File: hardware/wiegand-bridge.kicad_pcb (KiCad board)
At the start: 4 copper layers, 90 x 95 mm, 195 parts, among them J1 USB-C, J10 READER D0 D1, J11 READER LED BEEP, J12 GND IN3, J13 IN4 GND, J14 DC IN, J15 RELAY NC NO, J16 RELAY COM, J17 W5500, J18 QWIIC, J19 EXPANSION, J2 6-36V IN, J20 RS485 A B, J21 RS485 12V GND, J3 READER PWR, J4 LiFePO4 + NTC, J5 OLED SOCKET, J6 TFT/EPD, J8 TAMPER EXT, J9 IN1 IN2, K1 SRD-05VDC-SL-C, Q1 2N7002, Q10 2N7002, Q11 AO3401A, Q12 AO3400A, Q2 2N7002, Q4 2N7002, Q5 AO3401A, Q6 FS8205A, Q7 2N7002, Q8 2N7002, Q9 2N7002, SW1 BOOT, SW2 RESET, SW3 TAMPER, U1 ESP32-S3-WROOM-1-N8R2, U10 LMV321, U2 LMR16020, U3 TPS63001, U4 SN74LVC2G17, U5 CN3058E, U6 MT3608, U7 DW01A, U8 TCA9535, U9 SP3485

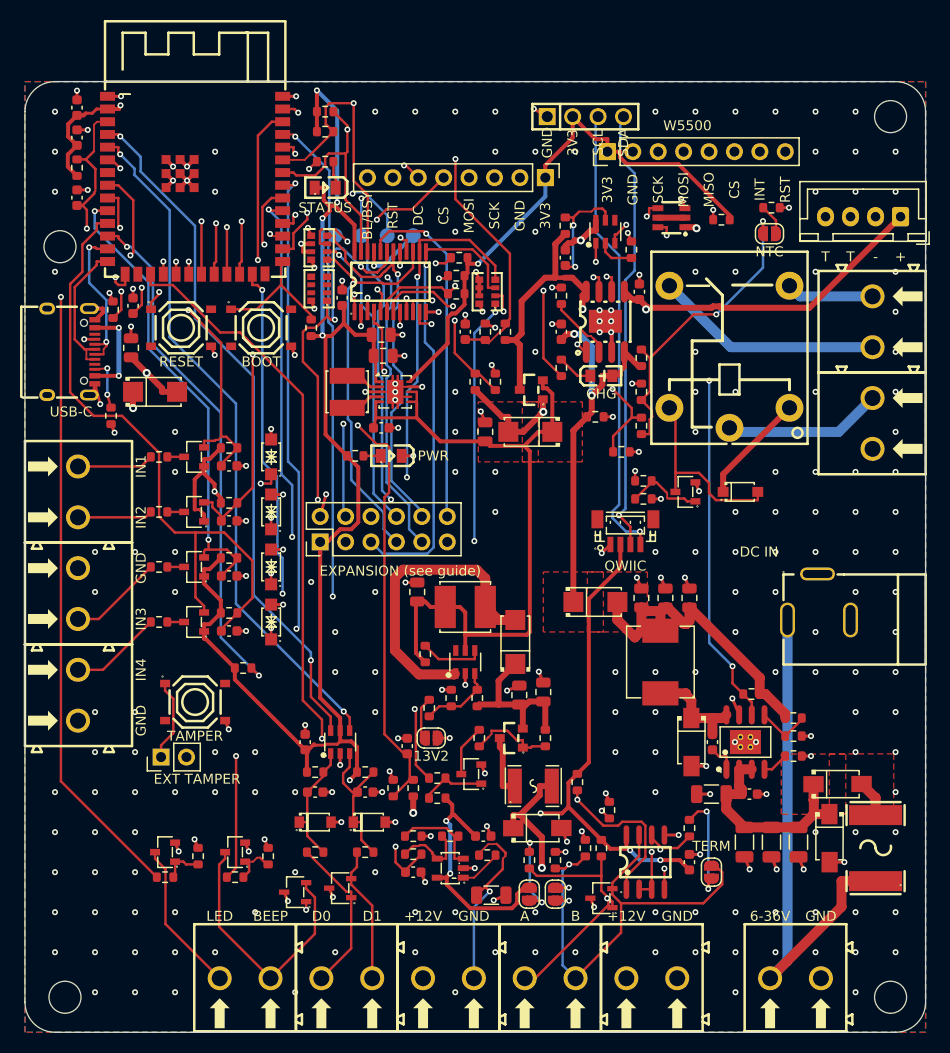
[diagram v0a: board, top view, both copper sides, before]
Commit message: Revision 11: red/green status pair and silkscreen legibility (routed and checked, not yet ordered)
Rev 10 is built and tested and stays available as tag rev-10b.
- D8 becomes red FAULT (IO21, ESPHome's status LED); new D23 green OK on IO47 via R81, lit while
  Home Assistant is connected. DISP_RST moves from IO47 to expander P06 (shared with J19 pin 3).
- Every silkscreen label held clear of pads, outlines, fitted parts and other text; audit.py --silk
  checks it (rev 10 had 41 problems in 70 labels). stitch.py keeps vias out of through-hole pads.
- Fab outputs and renders regenerated; the schematic PDF title now says revision 11.
- Firmware drives the OK LED (harmless on rev 10, where IO47 reaches only the unfitted J6).
- docs/design.md and README describe the changes.
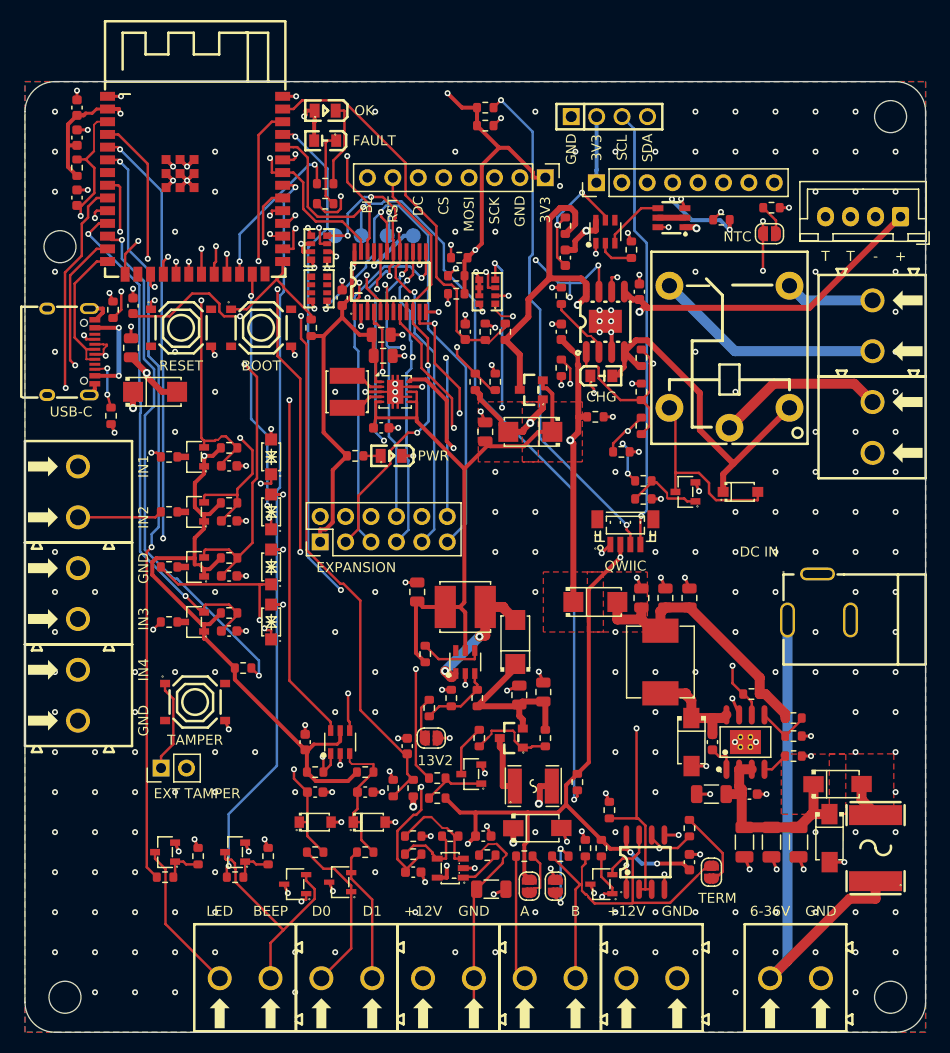
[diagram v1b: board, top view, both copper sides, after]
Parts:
- added D23: green, LED0805-R-RD, F.Cu at (130.0, 102.9)
- added R81: 1k, R_0603_1608Metric, F.Cu at (130.0, 110.2)
- D8: value yellow -> red; footprint LED0805-R-RD -> LED0805-RD
- moved R37 16.0 mm to (146.0, 104.4)
- moved R36 16.0 mm to (146.0, 102.6)
- moved D8 4.70 mm to (130.0, 105.9)
- moved R8 4.20 mm to (130.0, 112.2)
- moved J17 3.29 mm to (157.1, 110.1)
- moved J5 2.40 mm to (158.4, 103.5)
- moved D19 1.40 mm to (157.6, 180.2)
- moved J8 1.10 mm to (113.6, 168.6)
- moved R40 1.00 mm to (114.4, 137.5)
- moved R41 1.00 mm to (114.4, 143.0)
- moved R42 1.00 mm to (114.4, 148.5)
- moved R43 1.00 mm to (114.4, 154.0)
- moved D16 0.80 mm to (127.0, 180.2)
- moved JP3 0.80 mm to (150.4, 180.4)
- moved JP4 0.80 mm to (153.0, 180.4)
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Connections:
- D8 pad 1: +3V3 -> D8_K
- D8 pad 2: D8_K -> +3V3
- J19 pad 3: EXP06 -> DISP_RST
- RN1 pad 1: EXP06 -> DISP_RST
- U1 pad 24: DISP_RST -> IO47
- U8 pad 10: EXP06 -> DISP_RST
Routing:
- net EXP06: track 48.4 -> 0.00 mm, vias 3 -> 0
- net DISP_RST: track 23.6 -> 56.7 mm, vias 1 -> 3
- net BOOST_SW: track 30.5 -> 13.4 mm, vias 0 -> 2
- net IO47: track 0.00 -> 16.4 mm, vias 0 -> 2
- net RDR_ISENSE: track 75.2 -> 89.7 mm
- net PGOOD5: track 70.4 -> 57.6 mm, vias 3 -> 2
- net IN4: track 64.6 -> 51.9 mm, vias 0 -> 2
- net IN2: track 43.3 -> 55.0 mm
- net I2C_SDA: track 96.2 -> 107.8 mm, vias 2 -> 3
- net BAT_TEMP: track 57.8 -> 48.8 mm
- net RS485_DE: track 90.2 -> 98.9 mm
- net VSYS: track 73.4 -> 64.7 mm
- net D23_K: track 0.00 -> 8.60 mm
- net CHRG: track 39.4 -> 47.5 mm, vias 4 -> 6
- net IN4_RAW: track 31.4 -> 23.4 mm, vias 1 -> 2
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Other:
- board text added: "BL"
- board text added: "EXPANSION"
- board text added: "FAULT"
- board text added: "OK"
- board text added: "T T: 10k NTC"
- board text added: "rev 11 2026-10"
- board text removed: "BL/BSY"
- board text removed: "EXPANSION (see guide)"
- board text removed: "STATUS"
- board text removed: "T T: 10k B3950 NTC"
- board text removed: "rev 10b 2026-10"
